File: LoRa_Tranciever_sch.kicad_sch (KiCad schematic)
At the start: 16 parts, among them J3 Conn_Coaxial, U3 SX1280IMLTRT, Y1 52MHz

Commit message: Done power
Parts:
- removed U3: SX1280IMLTRT, footprints:QFN24_4X4_SEM, symbol RF_Parts:SX1280IMLTRT
- removed Y1: 52MHz, Crystal:Crystal_SMD_0603-4Pin_6.0x3.5mm, symbol Device:Crystal_GND3
- added C14, C15, C16, C17, C28, C29, C30, C31, C32, C33, C34, C36, C37, C38: C, symbol Device:C
- added C35: 1n, Capacitor_SMD:C_0402_1005Metric, symbol Device:C
- added L3, L4, L5, L6, L7, L8: L, symbol Device:L
- added R6: 100R, symbol Device:R
- added R7, R9: NC, symbol Device:R
- added R8: 1k, symbol Device:R
- added U5: SX1276IMLTRT, digikey-footprints:VQFN-28-1EP_6x6mm, symbol dk_RF-Transceiver-ICs:SX1276IMLTRT
- added U6: 4259-63, digikey-footprints:SOT-363, symbol dk_RF-Switches:4259-63
- added Y1: Crystal_GND24, symbol Device:Crystal_GND24
- C18, C27: value 100n -> C; footprint Capacitor_SMD:C_0402_1005Metric -> (none)
- C19: value 0.8p -> C; footprint Capacitor_SMD:C_0402_1005Metric -> (none)
- C20, C23: value 1p2 -> C; footprint Capacitor_SMD:C_0402_1005Metric -> (none)
- C21: value 0.5p -> C; footprint Capacitor_SMD:C_0402_1005Metric -> (none)
- C22: value 100p -> C; footprint Capacitor_SMD:C_0402_1005Metric -> (none)
- C24, C25: value 10n -> C; footprint Capacitor_SMD:C_0402_1005Metric -> (none)
- C26: value 470n -> C; footprint Capacitor_SMD:C_0402_1005Metric -> (none)
- J3: footprint footprints:TAOGLAS_EMPCB.SMAFSTJ.B.HT -> Connector_Coaxial:SMA_Amphenol_132289_EdgeMount; JLC # (none) -> C2987684
- L1: value 3n -> L; footprint Inductor_SMD:L_0402_1005Metric -> (none)
- L2: value 2n5 -> L; footprint Inductor_SMD:L_0402_1005Metric -> (none)
- R5: footprint Capacitor_SMD:C_0402_1005Metric -> (none)
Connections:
- net +3V3: now also C19.1, C15.1, C17.1, C34.1, R8.2, U5.14 (VBAT_DIG), U5.24 (VBAT_RF), U5.3 (VBAT_ANA), U6.6 (~{CTRL}/VDD); no longer R5.2
- net DIO1: now also U5.9 (DIO1/DCLK)
- net DIO2: now also U5.10 (DIO2/DATA)
- net DIO3: now also U5.11 (DIO3), U5.12 (DIO4), U5.13 (DIO5)
- net GND: now also C19.2, C20.1, C21.2, C22.2, C24.1, C26.1, C27.1, L2.2, C14.2, C15.2, C16.2, C17.2, C30.1, C33.1, C34.2, C35.2, C37.1, C38.1, R9.1, U5.15 (GND), U5.23 (GND), U5.25 (VR_PA), U5.26 (GND), U5.29 (GND), U6.2 (GND), Y1.2, Y1.4; no longer C19.1, C23.1, C27.2
- net MOSI_RX: now also U5.18 (MOSI)
- net NSS_CTS: now also U5.19 (NSS)
- net SCK_RTSN: now also U5.16 (SCK)
- net at C25.1: now also C28.1, L3.2; no longer C26.1
- net at J3.1 (In): now also C38.2, L8.2; no longer C22.2
- net at C21.1, L1.2, L2.1: now also C23.1; no longer C20.1
- net at L1.1: now also U5.27 (PA_BOOST); no longer C19.2
- net V DIO: no longer names the net of R5.1
- net V DIO: now also C28.2; no longer C27.1
- new net: C37.2, L7.2, L8.1
- new net: C16.1, U5.4 (VR_DIG)
- new net: C23.2, L4.1
- new net: C27.2, C29.2, L4.2, L5.1
- new net: C29.1, C30.2, C31.2, L5.2, L6.1
- new net: C31.1, C33.2, L6.2, U6.3 (RF2)
- new net: C14.1, U5.2 (VR_ANA)
- new net: U5.5 (XTA), Y1.3
- new net: U5.6 (XTB), Y1.1
- new net: C32.1, R5.2
- new net: C32.2, U6.1 (RF1)
- new net: C36.1, U6.5 (RFC)
- new net: C36.2, L7.1
- new net DIO0: U5.8 (DIO0)
- new net MISO_TX: U5.17 (MISO)
- new net RFI_HF: C22.1, L3.1, U5.21 (RFI_HF(GND))
- new net RXTX_EXT: R6.2, R8.1, R9.2
- new net RXTX_SW: C35.1, R6.1, R7.1, U6.4 (CTRL)
- new net RXTX_SX: R7.2, U5.20 (RXTX/RF_MOD)
- new net SX1276_NRESET: U5.7 (NRESET)
- no-connect marks 1 -> 3
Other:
- note added: "RF Switch makes Recieving sensitivty much higher"
- note added: "This design is based off the refrence design given by semtec for the sx1276 although that one has two antennas one for LF and HF we only use HF at 915MHz and we use PA_Boost for boost of 20dbm"
- note added: "We use the microcontroller to switch"

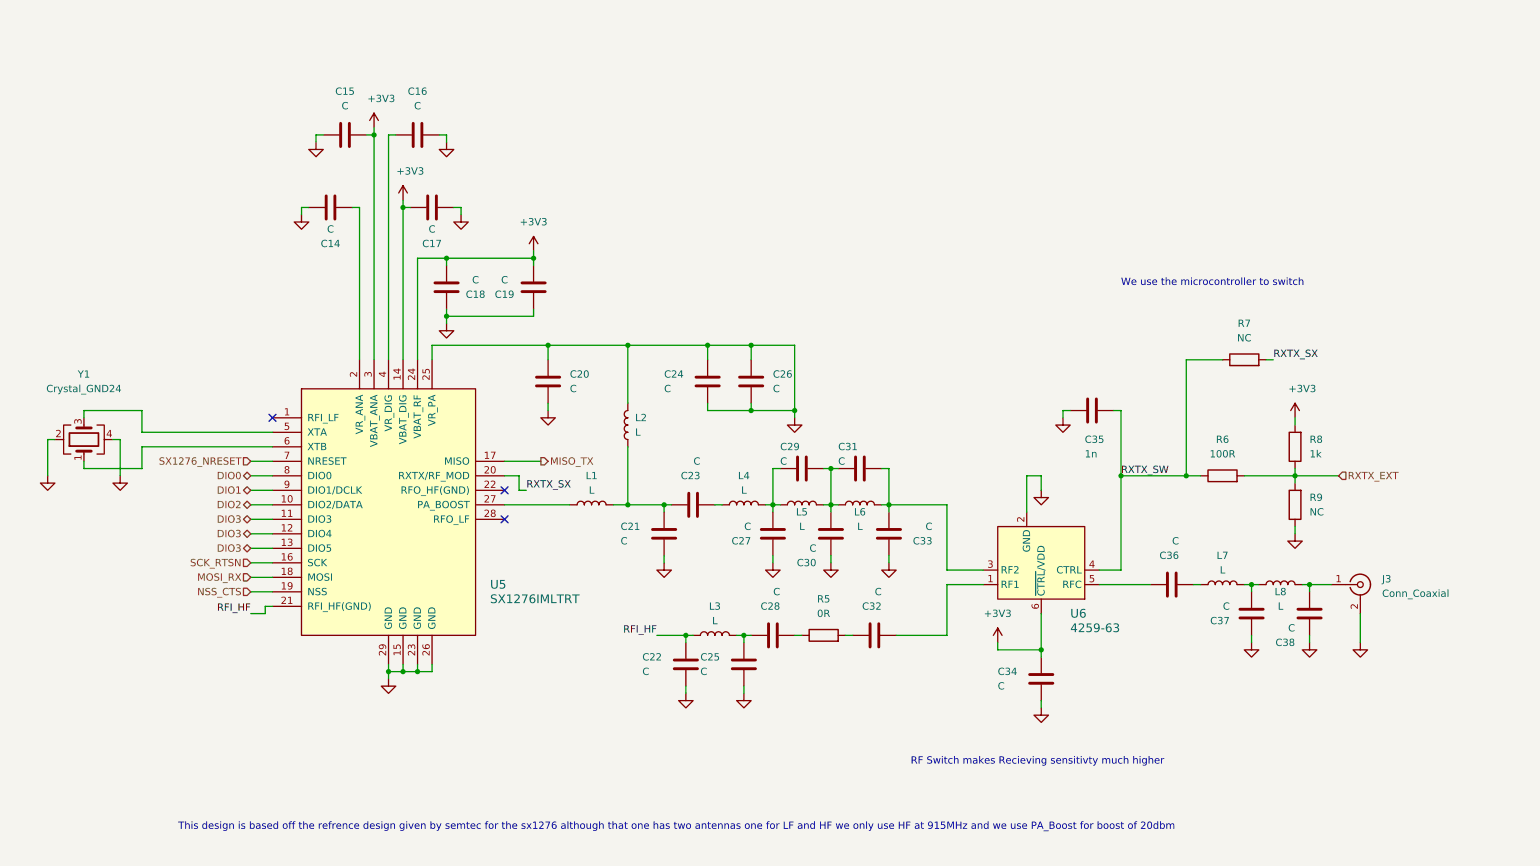
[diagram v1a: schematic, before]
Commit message: Added all schmatics about to change LDO 1 to buck
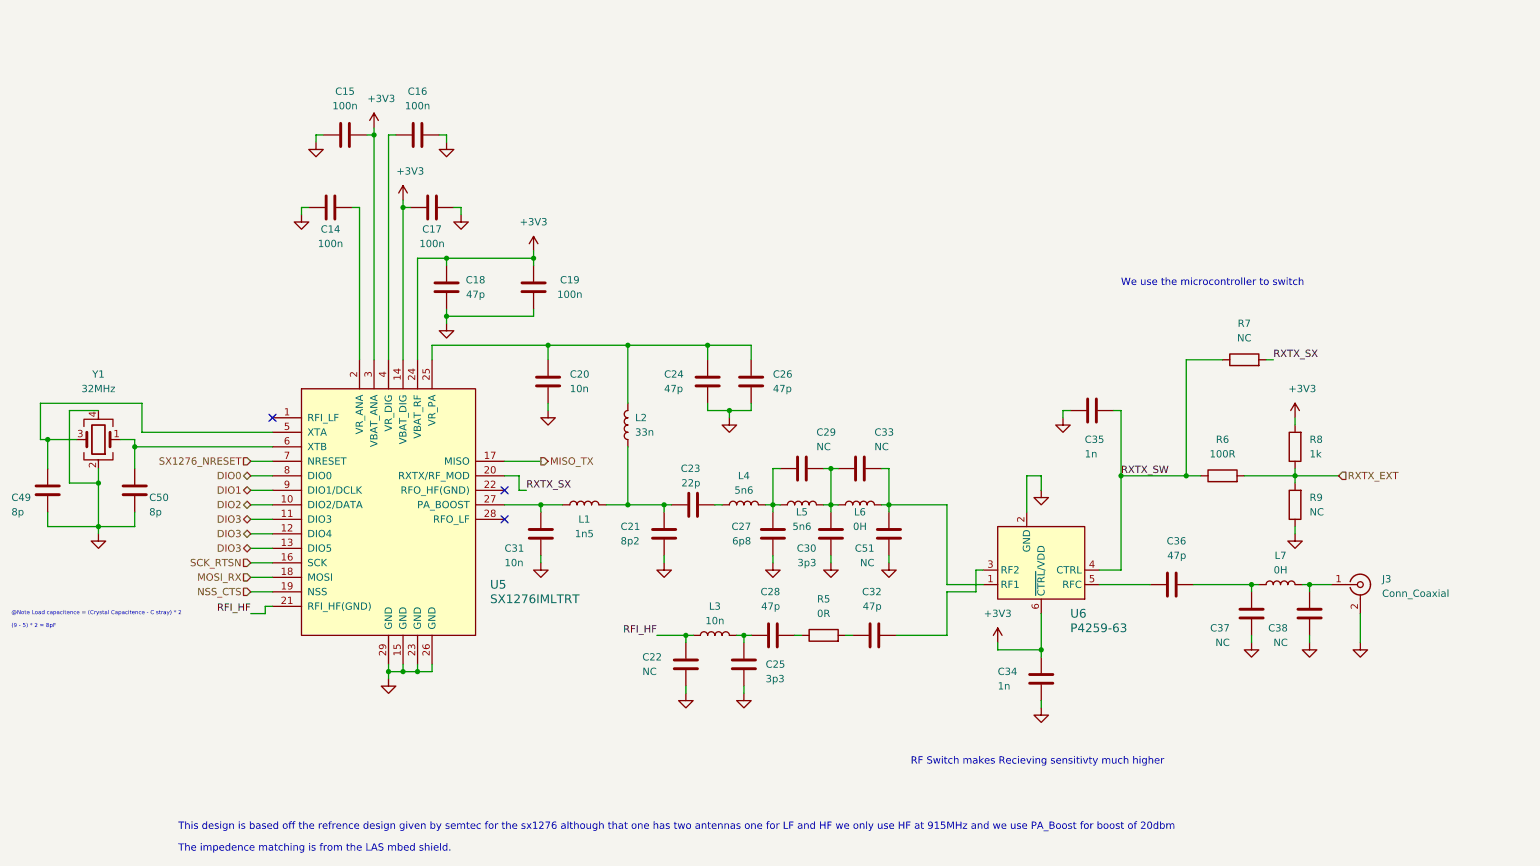
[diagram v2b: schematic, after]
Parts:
- removed L8: L, symbol Device:L
- added C49, C50: 8p, Capacitor_SMD:C_0402_1005Metric, symbol Device:C
- added C51: NC, Capacitor_SMD:C_0402_1005Metric, symbol Device:C
- C14, C15, C16, C17, C19: value C -> 100n; footprint (none) -> Capacitor_SMD:C_0402_1005Metric
- C18, C24, C26, C28, C32, C36: value C -> 47p; footprint (none) -> Capacitor_SMD:C_0402_1005Metric
- C20, C31: value C -> 10n; footprint (none) -> Capacitor_SMD:C_0402_1005Metric
- C21: value C -> 8p2; footprint (none) -> Capacitor_SMD:C_0402_1005Metric
- C22, C29, C33, C37, C38: value C -> NC; footprint (none) -> Capacitor_SMD:C_0402_1005Metric
- C23: value C -> 22p; footprint (none) -> Capacitor_SMD:C_0402_1005Metric
- C25, C30: value C -> 3p3; footprint (none) -> Capacitor_SMD:C_0402_1005Metric
- C27: value C -> 6p8; footprint (none) -> Capacitor_SMD:C_0402_1005Metric
- C34: value C -> 1n; footprint (none) -> Capacitor_SMD:C_0402_1005Metric
- L1: value L -> 1n5; footprint (none) -> Inductor_SMD:L_0402_1005Metric
- L2: value L -> 33n; footprint (none) -> Inductor_SMD:L_0402_1005Metric
- L3: value L -> 10n; footprint (none) -> Inductor_SMD:L_0402_1005Metric
- L4, L5: value L -> 5n6; footprint (none) -> Inductor_SMD:L_0402_1005Metric
- L6, L7: value L -> 0H; footprint (none) -> Inductor_SMD:L_0402_1005Metric
- R5, R6, R7, R8, R9: footprint (none) -> Resistor_SMD:R_0402_1005Metric
- U6: value 4259-63 -> P4259-63
- Y1: value Crystal_GND24 -> 32MHz; footprint (none) -> Crystal:Crystal_SMD_0603-4Pin_6.0x3.5mm; JLC Part # (none) -> C255895
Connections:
- net GND: now also C31.2, C49.2, C50.2, C51.1; no longer C20.1, C24.1, C26.1, C33.1, L2.2, U5.25 (VR_PA)
- net at C37.2: now also C36.2, L7.1; no longer L7.2
- net at C29.1, C30.2, L5.2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: now also C33.2; no longer C31.2
- net at C38.2, J3.1 (In): now also L7.2
- net at L1.1, U5.27 (PA_BOOST): now also C31.1
- net at U5.5 (XTA), Y1.3: now also C49.1
- net at U5.6 (XTB), Y1.1: now also C50.1
- net at U6.1 (RF1): now also C33.1, L6.2, C51.2; no longer C32.2
- new net: C20.1, C24.1, C26.1, L2.2, U5.25 (VR_PA)
- new net: C32.2, U6.3 (RF2)
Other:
- note added: "@Note Load capacitence = (Crystal Capacitence - C stray) * 2 (9 - 5) * 2 = 8pF"
- note added: "The impedence matching is from the LAS mbed shield."
- moved on the sheet: L7, Y1

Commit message: Done design
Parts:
- added C55, C57, C58: 1u, Capacitor_SMD:C_0402_1005Metric, symbol Device:C
- added C56: 22u, Capacitor_SMD:C_0603_1608Metric, symbol Device:C
- J3: footprint Connector_Coaxial:SMA_Amphenol_132289_EdgeMount -> footprints:TAOGLAS_EMPCB.SMAFSTJ.B.HT
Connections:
- net +3V3: now also C55.1, C56.1, C57.1, C58.1
- net DIO3: no longer U5.12 (DIO4), U5.13 (DIO5)
- net GND: now also C55.2, C56.2, C57.2, C58.2
- net RFO_HF: now reaches C31.1, L1.1, U5.27 (PA_BOOST)
- new net DIO4: U5.12 (DIO4)
- new net DIO5: U5.13 (DIO5)
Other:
- note added: "RF Shield 20 x 40 (+2mm)"
- moved on the sheet: C14, C15, C16, C17, C18, C19, C20, C21, C22, C23, C24, C25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

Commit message: a
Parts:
- C22, C29, C33, C37, C38, C51: now left out of the parts list
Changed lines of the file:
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@@
   )
   (symbol (lib_id "Device:C") (at 240.03 125.73 180) (unit 1)
-    (in_bom yes) (on_board yes) (dnp no)
+    (in_bom no) (on_board yes) (dnp no)
     (property "Reference" "C37" (at 236.22 128.27 0)
       (effects (font (size 1.27 1.27)) (justify left))
@@
   )
   (symbol (lib_id "Device:C") (at 171.45 100.33 270) (unit 1)
-    (in_bom yes) (on_board yes) (dnp no)
+    (in_bom no) (on_board yes) (dnp no)
     (property "Reference" "C33" (at 173.99 93.98 90)
       (effects (font (size 1.27 1.27)) (justify left))
@@
   )
   (symbol (lib_id "Device:C") (at 250.19 125.73 180) (unit 1)
-    (in_bom yes) (on_board yes) (dnp no)
+    (in_bom no) (on_board yes) (dnp no)
     (property "Reference" "C38" (at 246.38 128.27 0)
       (effects (font (size 1.27 1.27)) (justify left))
@@
   )
   (symbol (lib_id "Device:C") (at 176.53 111.76 180) (unit 1)
-    (in_bom yes) (on_board yes) (dnp no)
+    (in_bom no) (on_board yes) (dnp no)
     (property "Reference" "C51" (at 173.99 114.3 0)
       (effects (font (size 1.27 1.27)) (justify left))
@@
   )
   (symbol (lib_id "Device:C") (at 161.29 100.33 270) (unit 1)
-    (in_bom yes) (on_board yes) (dnp no)
+    (in_bom no) (on_board yes) (dnp no)
     (property "Reference" "C29" (at 163.83 93.98 90)
       (effects (font (size 1.27 1.27)) (justify left))
@@
   )
   (symbol (lib_id "Device:C") (at 140.97 134.62 0) (unit 1)
-    (in_bom yes) (on_board yes) (dnp no)
+    (in_bom no) (on_board yes) (dnp no)
     (property "Reference" "C22" (at 133.35 133.35 0)
       (effects (font (size 1.27 1.27)) (justify left))

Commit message: Added logo and assigned parts
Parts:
- C22: renamed from C14; JLC # (none) -> C327414
- C23: renamed from C15; JLC # (none) -> C327414
- C24: renamed from C16; JLC # (none) -> C327414
- C25: renamed from C17; JLC # (none) -> C327414
- C27: renamed from C19; JLC # (none) -> C327414
- C28: renamed from C31; JLC # (none) -> C183758
- C29: renamed from C20; JLC # (none) -> C183758
- J5: renamed from J3; LCSC # (none) -> C1509221
- U6: renamed from U5; DK_Datasheet_Link https://cdn.sparkfun.com/assets/a/a/0/b/5/DS_SX1276-7-8-9_W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 -> (none); DK_Detail_Page /product-detail/en/semtech-corporation/SX1276IMLTRT/SX1276I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 -> (none); Digi-Key_PN SX1276IMLTRTCT-ND -> (none); Family RF Transceiver ICs -> (none); LCSC # (none) -> C80171; MPN SX1276IMLTRT -> (none); Manufacturer Semtech Corporation -> (none); Status Active -> (none)
- U7: renamed from U6; DK_Datasheet_Link http://www.psemi.com/pdf/datasheets/pe4259ds.pdf -> (none); DK_Detail_Page /product-detail/en/psemi/4259-63/1046-1011-1-ND/2614515 -> (none); Digi-Key_PN 1046-1011-1-ND -> (none); Family RF Switches -> (none); LCSC # (none) -> C470892; MPN 4259-63 -> (none); Manufacturer pSemi -> (none); Status Active -> (none)
- Y1: footprint Crystal:Crystal_SMD_0603-4Pin_6.0x3.5mm -> Crystal:Crystal_SMD_2016-4Pin_2.0x1.6mm; JLC Part # C255895 -> (none); LCSC # (none) -> C1986260
- renumbered C49 to C20, C50 to C21, C18 to C26, C21 to C30, C23 to C31, C22 to C32, C24 to C33, C26 to C34, C25 to C35, C27 to C36, C55 to C37, C28 to C38, C29 to C39, C30 to C40, C33 to C41, C32 to C42, C51 to C43, C56 to C44, C34 to C45, C57 to C46, C35 to C47, C58 to C48, C36 to C49, C37 to C50, C38 to C51, R5 to R20, R6 to R21, R7 to R22, R8 to R23, R9 to R24
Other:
- moved on the sheet: C32, C35, C38, C42, L3, R20, Y1

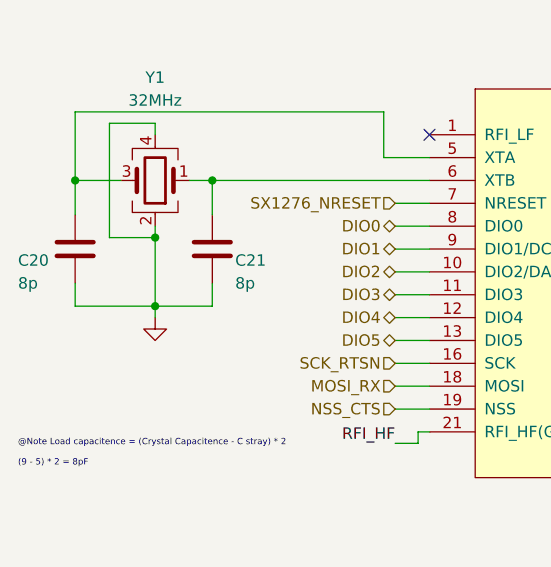
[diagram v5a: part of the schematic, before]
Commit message: Ready to order added all part numbers
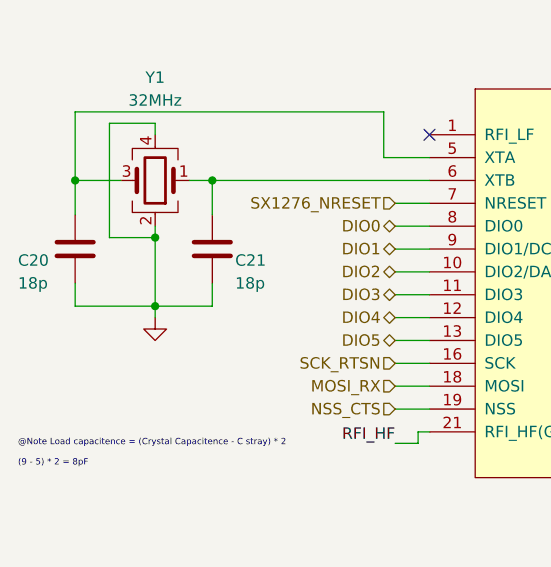
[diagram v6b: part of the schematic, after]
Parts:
- C20, C21: value 8p -> 18p; LCSC # (none) -> C1549
- C22, C23, C24, C25, C27: JLC # C327414 -> (none); LCSC # (none) -> C1525
- C26, C33, C34, C38, C42, C49: LCSC # (none) -> C1567
- C28, C29: JLC # C183758 -> (none); LCSC # (none) -> C3855387
- C30: LCSC # (none) -> C1579
- C31: LCSC # (none) -> C1555
- C35, C40: LCSC # (none) -> C2941931
- C36: LCSC # (none) -> C1576
- C37, C46, C48: LCSC # (none) -> C528974
- C44: LCSC # (none) -> C415703
- C45, C47: LCSC # (none) -> C106205
- J5: JLC # C2987684 -> (none)
- L1: LCSC # (none) -> C340346
- L2: LCSC # (none) -> C86062
- L3: LCSC # (none) -> C77103
- L4, L5: LCSC # (none) -> C91626
- L6, L7: LCSC # (none) -> C190119
- R20: LCSC # (none) -> C21189
- R21: LCSC # (none) -> C106233
- R23: LCSC # (none) -> C21190
- U6: JLC # C80171 -> (none)
- U7: JLC # C470892 -> (none)
